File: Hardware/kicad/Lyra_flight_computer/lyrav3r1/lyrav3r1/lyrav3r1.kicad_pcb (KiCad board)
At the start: 4 copper layers, 25 x 55 mm, 92 parts, among them IC1 TESEO-LIV3F, J1 Conn_01x02, J2 Screw_Terminal_01x02, J4 Conn_01x02, J5 Conn_01x05, J7 USB_B_Micro, J8 Screw_Terminal_01x07, Q1 AO3401A, Q10 AO3400A, Q11 Q_NPN_BEC, Q2 AO3400A, Q3 AO3400A, Q4 AO3400A, Q5 AO3400A, Q7 AO3400A, Q8 AO3400A, Q9 AO3400A, U1 E22-900MM22S, U2 BMI088, U3 BMP388, U4 LIS3MDLTR, U5 ADXL375BCCZ-RL7, U6 RT9013-33GB_C19268157, U7 WS7916S-6/TR, U8 RP2040, U9 W25Q128JVS, X2 SX1M12.000M10F30TNN

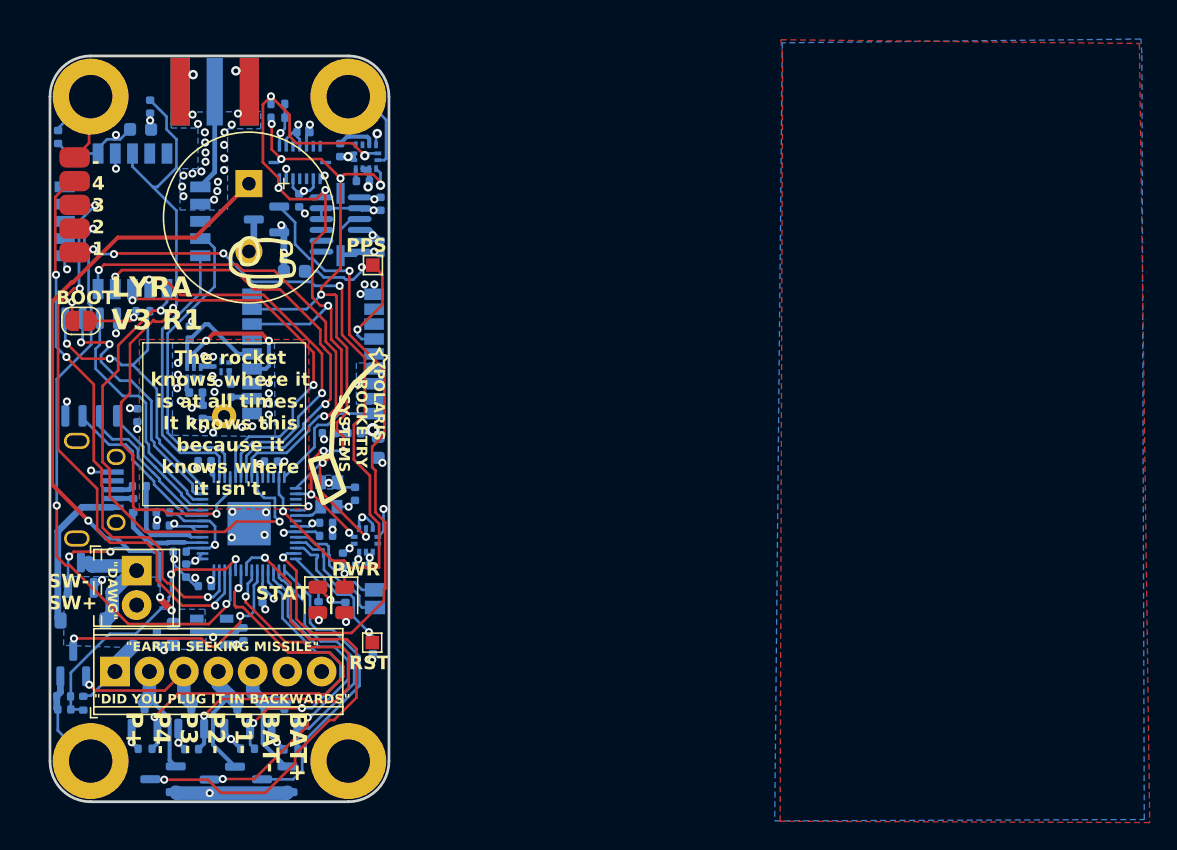
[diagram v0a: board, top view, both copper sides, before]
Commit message: added batt protection for lyra, added more parts for reciver
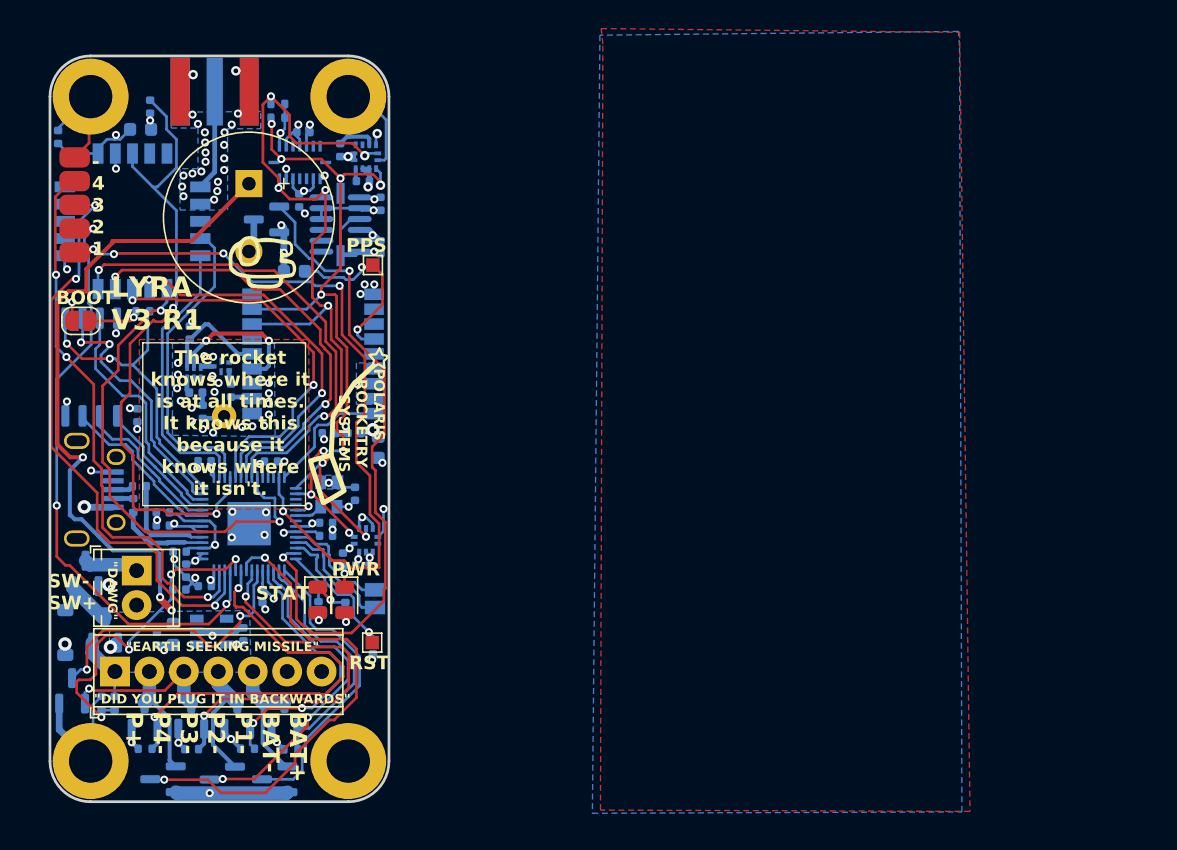
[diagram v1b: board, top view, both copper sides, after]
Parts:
- added Q6: AO3401A, Package_TO_SOT_SMD:SOT-23, B.Cu at (186.2, 102.2)
- moved C3 12.3 mm to (193.1, 103.4), turned to 0 degrees
- moved Q1 4.42 mm to (187.7, 106.4)
- moved R4 2.84 mm to (187.4, 111.8), turned to 90 degrees
- moved R2 2.31 mm to (188.4, 111.8)
- moved Q8 2.01 mm to (185.2, 110.8)
- moved D1 1.57 mm to (184.7, 106.6), turned to -90 degrees
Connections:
- D1 pad 1: /BATT POSTSW -> Net-(D1-K)
- Q1 pad 3: /BATT POSTSW -> Net-(D1-K)
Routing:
- net Net-(D1-K): track 0.00 -> 5.40 mm
- net VBUS: track 11.4 -> 16.0 mm, vias 0 -> 3
- net /BATT POSTSW: track 8.58 -> 4.07 mm
- net +BATT: track 57.8 -> 53.6 mm, vias 5 -> 3
- net GND: track 95.9 -> 99.3 mm
- net /BATT SENSE : track 21.2 -> 24.1 mm, vias 2 -> 4
- net /P3 CONT : track 18.0 -> 20.9 mm
- added copper zone on In2.Cu, net /BATT RAW
- removed copper zone on In1.Cu, net /BATT RAW

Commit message: reciver work and finalized lyrav3r1
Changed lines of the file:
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@@
 		(tags "capacitor")
 		(property "Reference" "C3"
-			(at 0 1.16 360)
+			(at 0 1.16 0)
 			(layer "B.SilkS")
 			(hide yes)
@@
 		)
 		(property "Value" "100n"
-			(at 0 -1.16 360)
+			(at 0 -1.16 0)
 			(layer "B.Fab")
 			(effects
@@
 		)
 		(fp_text user "${REFERENCE}"
-			(at 0 0 360)
+			(at 0 0 0)
 			(layer "B.Fab")
 			(effects
@@
 		(tags "SOT TO_SOT_SMD")
 		(property "Reference" "Q1"
-			(at 0 2.4 270)
+			(at 0 2.4 -90)
 			(layer "B.SilkS")
 			(hide yes)
@@
 		)
 		(property "Value" "AO3401A"
-			(at 0 -2.4 270)
+			(at 0 -2.4 -90)
 			(layer "B.Fab")
 			(effects
@@
 		)
 		(fp_text user "${REFERENCE}"
-			(at 0 0 270)
+			(at 0 0 -90)
 			(layer "B.Fab")
 			(effects
@@
 		(tags "SOT TO_SOT_SMD")
 		(property "Reference" "Q6"
-			(at 0 2.4 270)
+			(at 0 2.4 -90)
 			(layer "B.SilkS")
 			(hide yes)
@@
 		)
 		(property "Value" "AO3401A"
-			(at 0 -2.4 270)
+			(at 0 -2.4 -90)
 			(layer "B.Fab")
 			(effects
@@
 		)
 		(fp_text user "${REFERENCE}"
-			(at 0 0 270)
+			(at 0 0 -90)
 			(layer "B.Fab")
 			(effects
@@
 		(tags "resistor")
 		(property "Reference" "R4"
-			(at 0 1.17 270)
+			(at 0 1.17 -90)
 			(layer "B.SilkS")
 			(hide yes)
@@
 		)
 		(property "Value" "40k"
-			(at 0 -1.17 270)
+			(at 0 -1.17 -90)
 			(layer "B.Fab")
 			(effects
@@
 		)
 		(fp_text user "${REFERENCE}"
-			(at 0 0 270)
+			(at 0 0 -90)
 			(layer "B.Fab")
 			(effects
@@
 		(polygon
 			(pts
-				(xy 224.246007 62.005299) (xy 250.687407 62.284699) (xy 251.449407 119.739499) (xy 224.195207 119.637899)
-				(xy 224.373007 63.148299)
+				(xy 182.5752 61.8998) (xy 209.0166 62.1792) (xy 209.7786 119.634) (xy 182.5244 119.5324) (xy 182.7022 63.0428)
 			)
 		)
@@
 		(polygon
 			(pts
-				(xy 250.598799 62.215744) (xy 224.157399 62.495144) (xy 223.598599 119.873744) (xy 250.852799 119.772144)
-				(xy 250.674999 63.282544)
+				(xy 208.915 62.6618) (xy 182.4736 62.9412) (xy 181.9148 120.3198) (xy 209.169 120.2182) (xy 208.9912 63.7286)
 			)
 		)

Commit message: work, lyra mostly final
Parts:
- added R5: 100R, Resistor_SMD:R_0402_1005Metric, B.Cu at (202.0, 77.0)
- added R6: 100k, Resistor_SMD:R_0402_1005Metric, B.Cu at (199.4, 107.7)
- added R7: 100k, Resistor_SMD:R_0402_1005Metric, B.Cu at (200.0, 115.1)
- added R8: 100k, Resistor_SMD:R_0402_1005Metric, B.Cu at (196.3, 115.1)
- added R9: 100k, Resistor_SMD:R_0402_1005Metric, B.Cu at (192.4, 115.1)
- D1: value D -> D_Schottky; footprint Diode_SMD:D_SOD-123 -> Diode_SMD:D_SOD-323F
- moved R17 0.53 mm to (201.9, 115.1)
- moved Q10 0.39 mm to (191.5, 117.4)
- moved R11 0.24 mm to (194.3, 115.1)
- moved D1 0.14 mm to (184.7, 106.4)
- moved R12 0.12 mm to (190.5, 115.1)
- turned D3 to 90 degrees
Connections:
- D3 pad 1: +3V3 -> Net-(D3-K)
- D3 pad 2: Net-(D3-A) -> +3V3
- Q11 pad 1: /BUZZER -> Net-(Q11-B)
- R28 pad 2: Net-(D3-A) -> Net-(D3-K)
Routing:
- net GND: track 99.3 -> 108.2 mm, vias 88 -> 83
- net /P3-: track 11.4 -> 18.8 mm, vias 1 -> 2
- net /SCL: track 53.8 -> 58.1 mm
- net +3V3: track 54.0 -> 57.3 mm
- net /BUZZER: track 48.2 -> 45.1 mm
- net /P1 CONT : track 22.7 -> 25.0 mm, vias 0 -> 2
- net Net-(Q11-B): track 0.00 -> 2.08 mm
- net /P4 CONT : track 34.7 -> 36.3 mm
- net Net-(D3-K): track 0.00 -> 0.94 mm, vias 0 -> 1
- net Net-(D3-A): track 0.94 -> 0.00 mm, vias 1 -> 0
- net VBUS: track 16.0 -> 16.7 mm
- net /P1-: track 9.72 -> 10.3 mm
- added copper zone on In1.Cu, net +3V3
- added copper zone on In1.Cu, net /BATT RAW
- added copper zone on In2.Cu, net GND
- removed copper zone on B.Cu, net (none)
- removed copper zone on F.Cu, net (none)
- removed copper zone on In2.Cu, net +3V3
- removed copper zone on In2.Cu, net /BATT RAW
- removed copper zone on In1.Cu, net GND

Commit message: stuffs
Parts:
- removed Q11: Q_NPN_BEC, Package_TO_SOT_SMD:SOT-23
- removed R5: 100R, Resistor_SMD:R_0402_1005Metric
- R2: value 20k -> 30k
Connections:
- BZ1 pad 1: +BATT -> /BUZZER
- BZ1 pad 2: Net-(BZ1--) -> GND
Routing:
- net +BATT: track 53.6 -> 4.84 mm, vias 3 -> 0
- net /BUZZER: track 45.1 -> 50.8 mm
- net Net-(BZ1--): track 2.51 -> 0.00 mm
- net Net-(Q11-B): track 2.08 -> 0.00 mm
- net GND: track 108.2 -> 107.9 mm, vias 83 -> 81

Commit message: post order omcmit
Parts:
- added TP3: TestPoint, TestPoint:TestPoint_Pad_1.0x1.0mm, F.Cu at (201.4, 65.5)
- added TP4: TestPoint, TestPoint:TestPoint_Pad_1.0x1.0mm, F.Cu at (205.6, 75.3)
- added TP5: TestPoint, TestPoint:TestPoint_Pad_1.0x1.0mm, F.Cu at (191.1, 78.9)
- added TP6: TestPoint, TestPoint:TestPoint_Pad_1.0x1.0mm, F.Cu at (194.1, 81.2)
- added TP7: TestPoint, TestPoint:TestPoint_Pad_1.0x1.0mm, F.Cu at (196.3, 82.5)
- moved AE3 0.35 mm to (196.1, 66.7)
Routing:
- net /SDA: track 63.6 -> 65.8 mm
- net /BRKOUT1: track 54.7 -> 55.8 mm
